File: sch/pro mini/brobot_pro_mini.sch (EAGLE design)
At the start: 31 parts, among them J1 MICRO_USB_B_MALE_HIROSE_ZX80-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, Q4 8MHz, U1 ATMEGA328L, U2 ###V

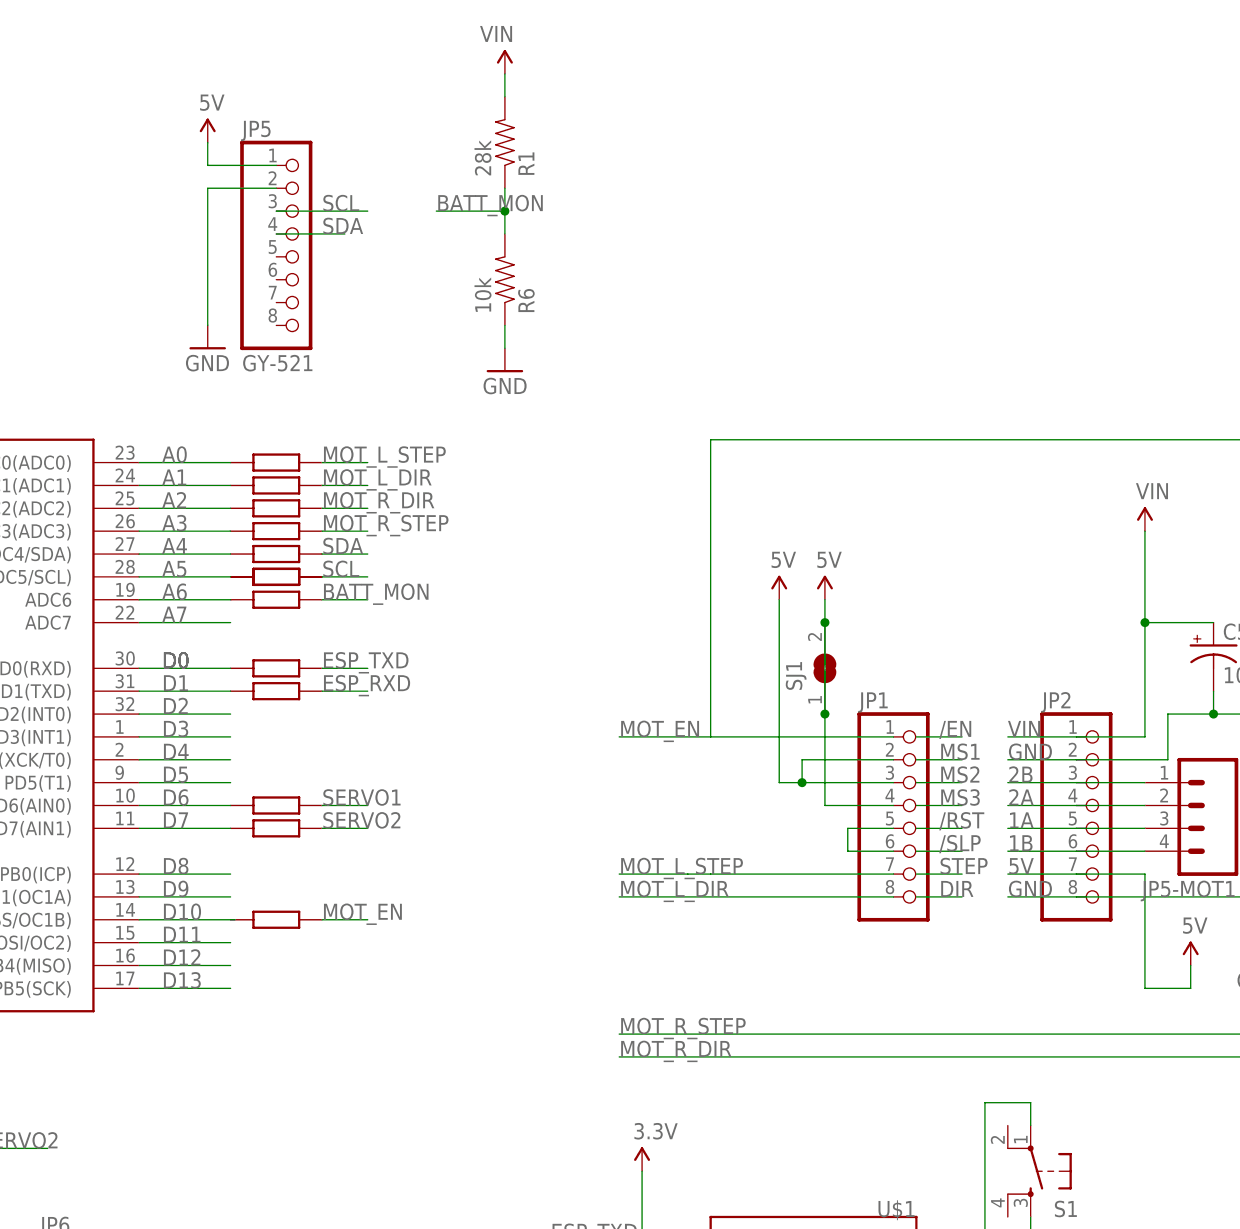
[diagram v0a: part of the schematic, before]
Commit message: battery monitor implementation
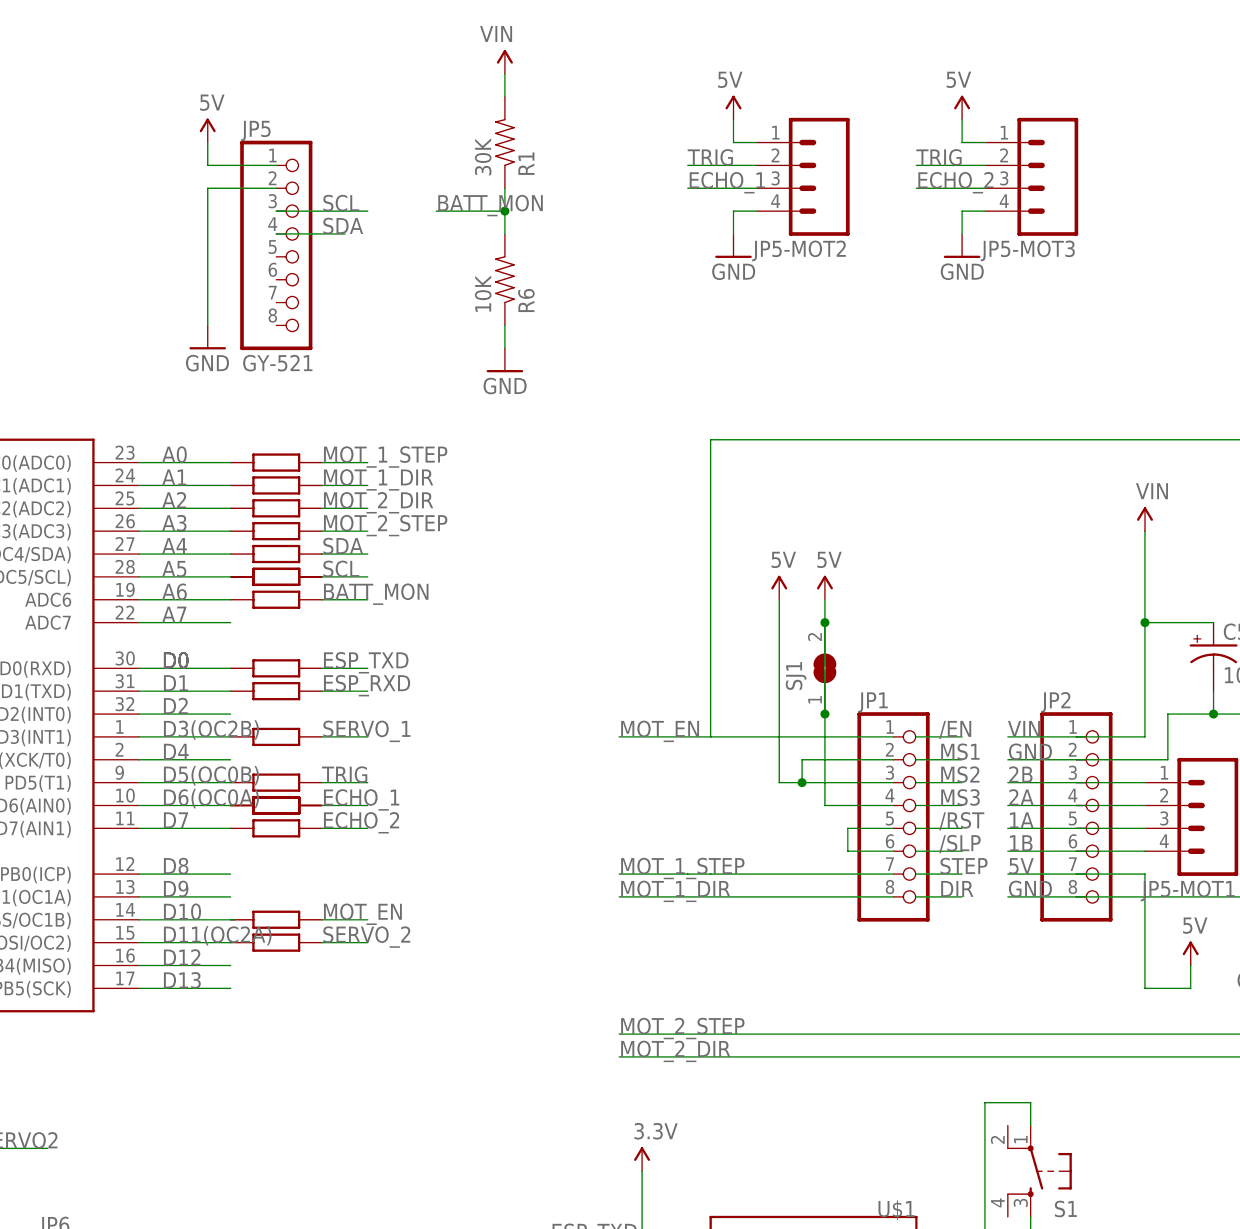
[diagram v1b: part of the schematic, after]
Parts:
- added JP5-MOT2, JP5-MOT3: (no value), SparkFun-Connectors:M04PTH
- R1: value 28k -> 30K
- R6: value 10k -> 10K
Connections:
- net D11 renamed D11(OC2A)
- net D3 renamed D3(OC2B)
- net D5 renamed D5(OC0B)
- net D6 renamed D6(OC0A)
- net MOT_L_DIR renamed MOT_1_DIR
- net MOT_L_STEP renamed MOT_1_STEP
- net MOT_R_DIR renamed MOT_2_DIR
- net MOT_R_STEP renamed MOT_2_STEP
- new net ECHO_1: JP5-MOT2.3
- new net ECHO_2: JP5-MOT3.3
- new net TRIG: JP5-MOT2.2, JP5-MOT3.2
- net 5V: now also JP5-MOT2.1, JP5-MOT3.1
- net GND: now also JP5-MOT2.4, JP5-MOT3.4

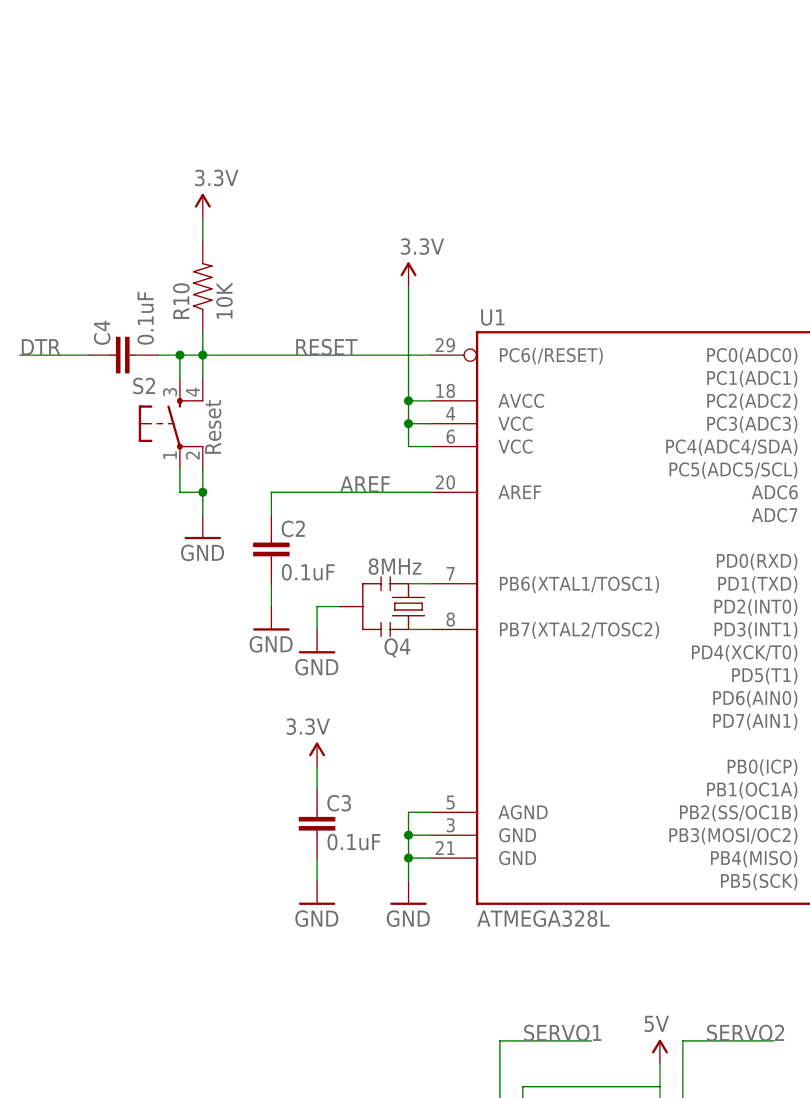
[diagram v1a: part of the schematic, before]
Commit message: esp8266 at command processor added
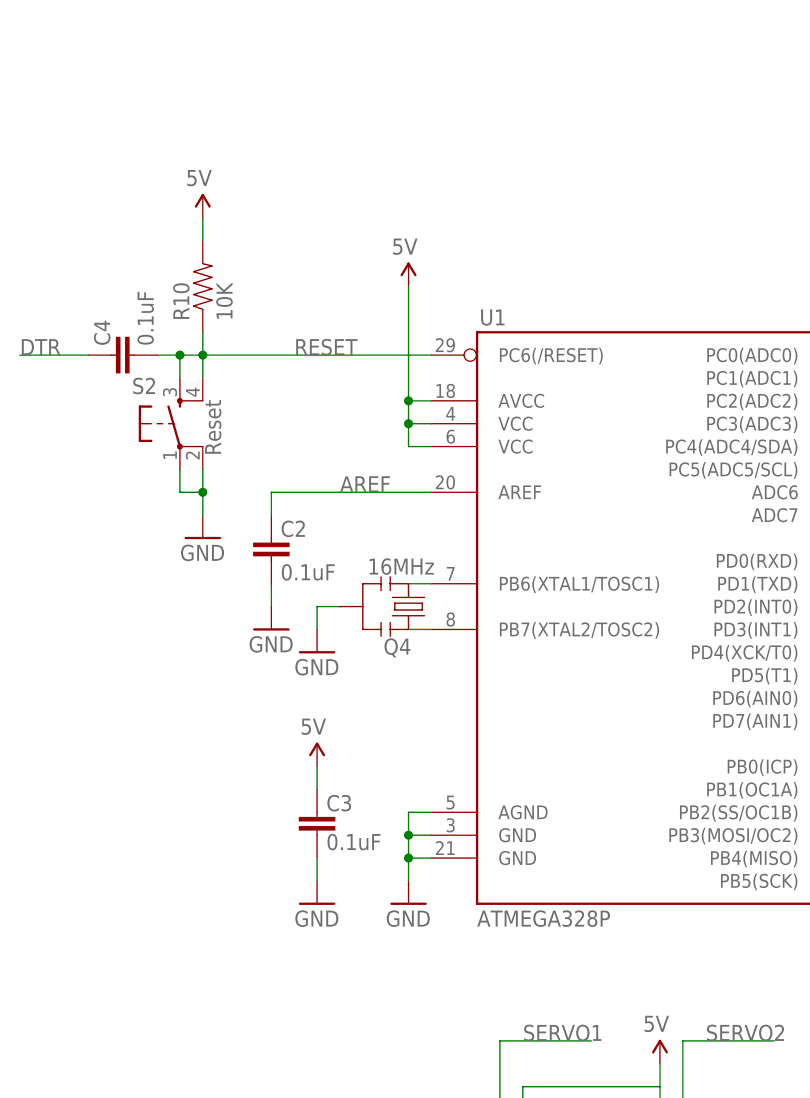
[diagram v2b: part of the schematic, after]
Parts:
- Q4: value 8MHz -> 16MHz
- U1: value ATMEGA328L -> ATMEGA328P
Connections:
- net 5V: now also C3.2, R10.2, U1.AVCC, U1.VCC@1, U1.VCC@2
- net VCC: no longer C3.2, R10.2, U1.AVCC, U1.VCC@1, U1.VCC@2
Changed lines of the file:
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@@
 <part name="C2" library="SparkFun" deviceset="CAP" device="0402" value="0.1uF"/>
 <part name="GND7" library="SparkFun" deviceset="GND" device=""/>
-<part name="P+11" library="SparkFun" deviceset="3.3V" device="" value="3.3V"/>
-<part name="P+15" library="SparkFun" deviceset="3.3V" device="" value="3.3V"/>
-<part name="Q4" library="SparkFun" deviceset="RESONATOR" device="SMD" value="8MHz"/>
+<part name="Q4" library="SparkFun" deviceset="RESONATOR" device="SMD" value="16MHz"/>
 <part name="GND4" library="SparkFun" deviceset="GND" device=""/>
-<part name="U1" library="SparkFun" deviceset="ATMEGA168" device="" value="ATMEGA328L"/>
-<part name="P+1" library="SparkFun" deviceset="3.3V" device="" value="3.3V"/>
+<part name="U1" library="SparkFun" deviceset="ATMEGA168" device="" value="ATMEGA328P"/>
 <part name="GND5" library="SparkFun" deviceset="GND" device=""/>
 <part name="C4" library="SparkFun" deviceset="CAP" device="0402" value="0.1uF"/>
@@
 <part name="R21" library="docu-dummy" deviceset="R" device=""/>
 <part name="R22" library="docu-dummy" deviceset="R" device=""/>
+<part name="SUPPLY14" library="SparkFun-Aesthetics" deviceset="5V" device=""/>
+<part name="SUPPLY15" library="SparkFun-Aesthetics" deviceset="5V" device=""/>
+<part name="SUPPLY16" library="SparkFun-Aesthetics" deviceset="5V" device=""/>
 </parts>
 <sheets>
@@
 </instance>
 <instance part="GND7" gate="1" x="78.74" y="139.7"/>
-<instance part="P+11" gate="G$1" x="71.12" y="185.42"/>
-<instance part="P+15" gate="G$1" x="83.82" y="124.46" smashed="yes">
-<attribute name="VALUE" x="80.264" y="128.016" size="1.778" layer="96"/>
-</instance>
 <instance part="Q4" gate="G$1" x="93.98" y="142.24" smashed="yes" rot="MR90">
 <attribute name="NAME" x="91.186" y="138.684" size="1.778" layer="95" rot="MR180"/>
@@
 <attribute name="VALUE" x="101.6" y="106.68" size="1.778" layer="96"/>
 </instance>
-<instance part="P+1" gate="G$1" x="93.98" y="177.8"/>
 <instance part="GND5" gate="1" x="93.98" y="109.22"/>
 <instance part="C4" gate="G$1" x="60.96" y="170.18" smashed="yes" rot="R270">
@@
 <instance part="R21" gate="G$1" x="160.02" y="132.08"/>
 <instance part="R22" gate="G$1" x="160.02" y="134.62"/>
+<instance part="SUPPLY14" gate="G$1" x="93.98" y="177.8" rot="MR0"/>
+<instance part="SUPPLY15" gate="G$1" x="71.12" y="185.42" rot="MR0"/>
+<instance part="SUPPLY16" gate="G$1" x="83.82" y="124.46" rot="MR0"/>
 </instances>
 <busses>
@@
 <nets>
 <net name="VCC" class="0">
-<segment>
-<wire x1="71.12" y1="185.42" x2="71.12" y2="182.88" width="0.1524" layer="91"/>
-<pinref part="R10" gate="G$1" pin="2"/>
-<pinref part="P+11" gate="G$1" pin="3.3V"/>
-</segment>
-<segment>
-<wire x1="83.82" y1="124.46" x2="83.82" y2="121.92" width="0.1524" layer="91"/>
-<pinref part="C3" gate="G$1" pin="2"/>
-<pinref part="P+15" gate="G$1" pin="3.3V"/>
-</segment>
-<segment>
-<wire x1="96.52" y1="165.1" x2="93.98" y2="165.1" width="0.1524" layer="91"/>
-<wire x1="93.98" y1="165.1" x2="93.98" y2="177.8" width="0.1524" layer="91"/>
-<wire x1="96.52" y1="162.56" x2="93.98" y2="162.56" width="0.1524" layer="91"/>
-<wire x1="93.98" y1="162.56" x2="93.98" y2="165.1" width="0.1524" layer="91"/>
-<wire x1="96.52" y1="160.02" x2="93.98" y2="160.02" width="0.1524" layer="91"/>
-<wire x1="93.98" y1="160.02" x2="93.98" y2="162.56" width="0.1524" layer="91"/>
-<junction x="93.98" y="165.1"/>
-<junction x="93.98" y="162.56"/>
-<pinref part="U1" gate="G$1" pin="AVCC"/>
-<pinref part="U1" gate="G$1" pin="VCC@1"/>
-<pinref part="U1" gate="G$1" pin="VCC@2"/>
-<pinref part="P+1" gate="G$1" pin="3.3V"/>
-</segment>
 <segment>
 <wire x1="132.08" y1="30.48" x2="137.16" y2="30.48" width="0.1524" layer="91"/>
@@
 <wire x1="236.22" y1="205.74" x2="238.76" y2="205.74" width="0.1524" layer="91"/>
 </segment>
-</net>
+<segment>
+<wire x1="96.52" y1="165.1" x2="93.98" y2="165.1" width="0.1524" layer="91"/>
+<wire x1="93.98" y1="165.1" x2="93.98" y2="177.8" width="0.1524" layer="91"/>
+<wire x1="96.52" y1="162.56" x2="93.98" y2="162.56" width="0.1524" layer="91"/>
+<wire x1="93.98" y1="162.56" x2="93.98" y2="165.1" width="0.1524" layer="91"/>
+<wire x1="96.52" y1="160.02" x2="93.98" y2="160.02" width="0.1524" layer="91"/>
+<wire x1="93.98" y1="160.02" x2="93.98" y2="162.56" width="0.1524" layer="91"/>
+<junction x="93.98" y="165.1"/>
+<junction x="93.98" y="162.56"/>
+<pinref part="U1" gate="G$1" pin="AVCC"/>
+<pinref part="U1" gate="G$1" pin="VCC@1"/>
+<pinref part="U1" gate="G$1" pin="VCC@2"/>
+<pinref part="SUPPLY14" gate="G$1" pin="5V"/>
+</segment>
+<segment>
+<wire x1="71.12" y1="185.42" x2="71.12" y2="182.88" width="0.1524" layer="91"/>
+<pinref part="R10" gate="G$1" pin="2"/>
+<pinref part="SUPPLY15" gate="G$1" pin="5V"/>
+</segment>
+<segment>
+<wire x1="83.82" y1="124.46" x2="83.82" y2="121.92" width="0.1524" layer="91"/>
+<pinref part="C3" gate="G$1" pin="2"/>
+<pinref part="SUPPLY16" gate="G$1" pin="5V"/>
+</segment>
+</net>
